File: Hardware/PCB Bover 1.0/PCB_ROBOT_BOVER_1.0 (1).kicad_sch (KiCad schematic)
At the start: 34 parts, among them J1 HC_SRO4, J10 KY_032, J2 HC_SRO4, J3 HC_SRO4, J4 HC_SRO4, J5 Alimentacion, J7 M1, J8 M2, J9 KY_032, U1 L298N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

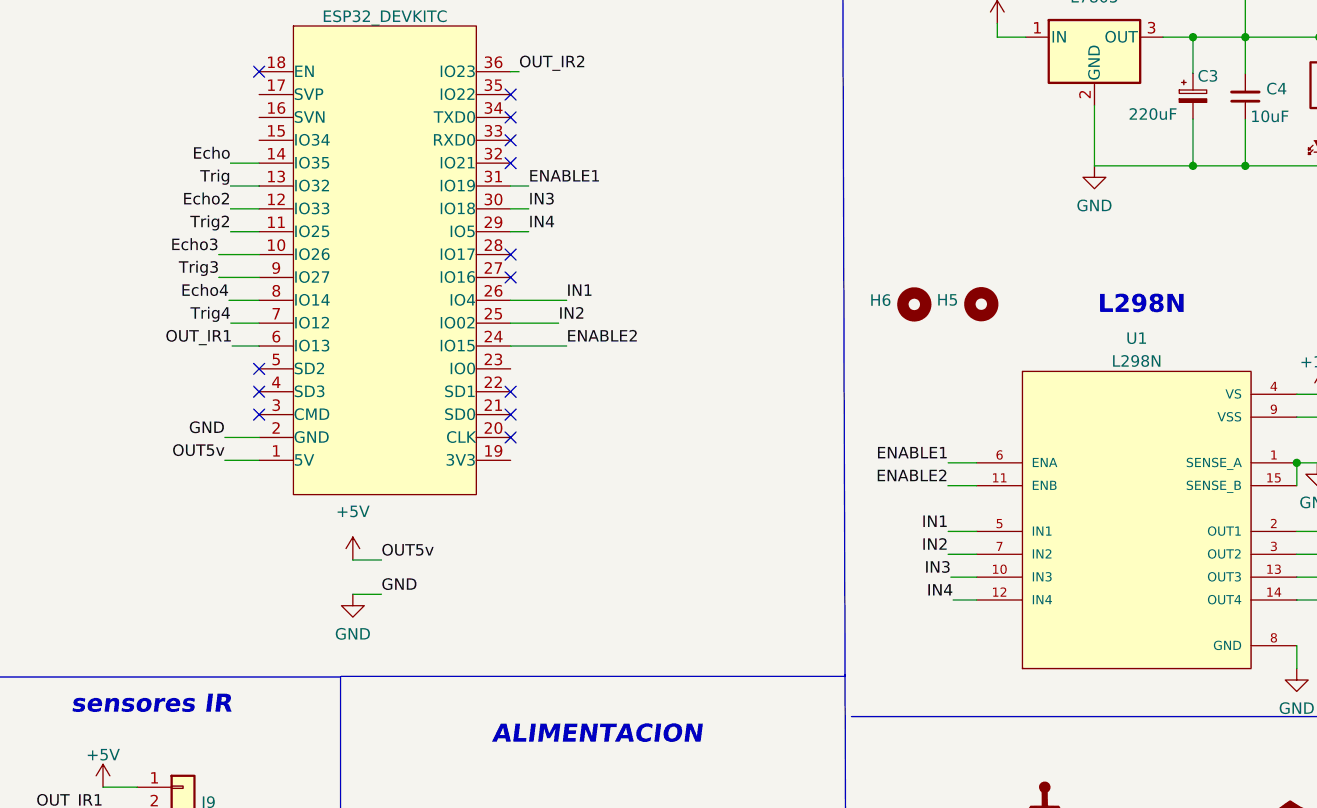
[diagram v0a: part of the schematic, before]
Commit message: add the designs and PCB edit
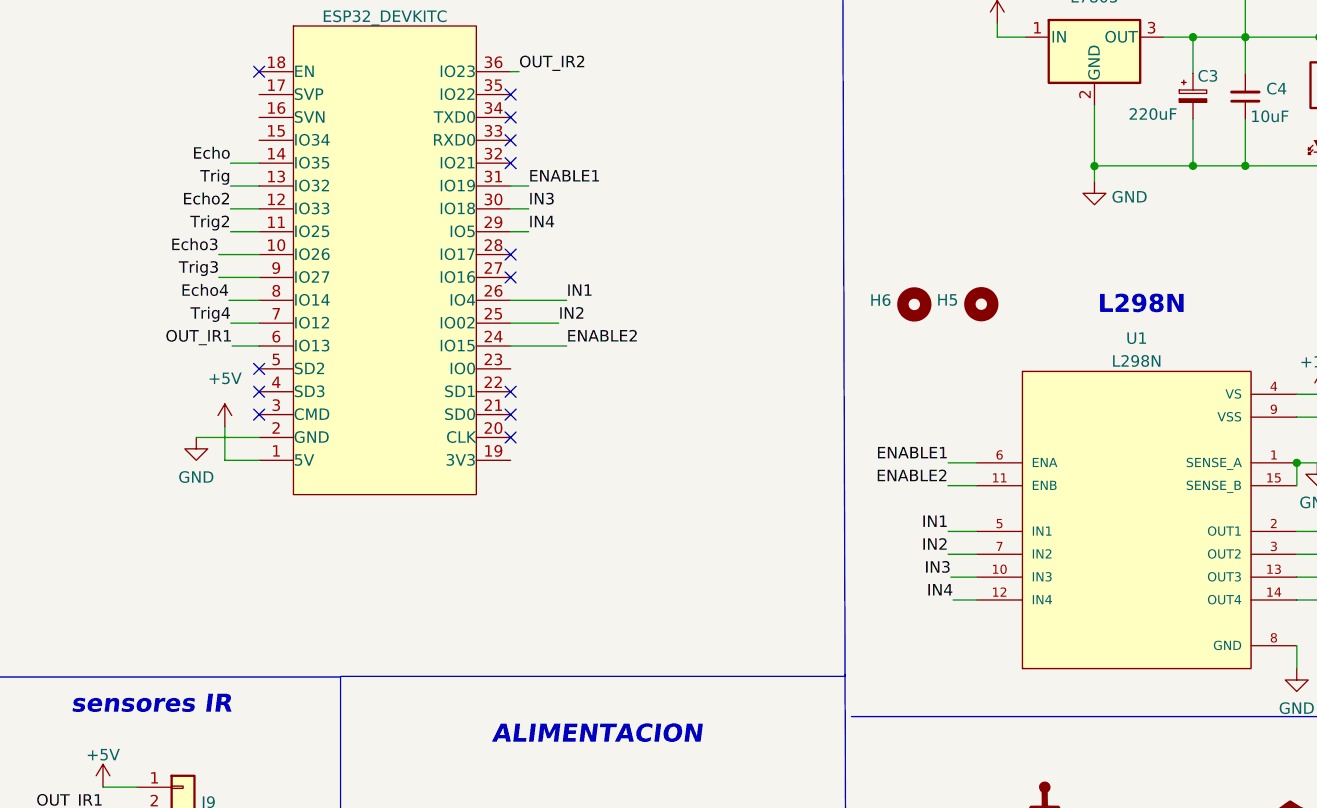
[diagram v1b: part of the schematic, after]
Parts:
- G2: value (none) -> LOGO RB EXP 1.0; footprint (none) -> robot logos:logo rb exp
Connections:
- net GND: no longer C3.2, C4.1, LED1.2 (K), U2.2 (GND)
- new net: C3.2, C4.1, LED1.2 (K), U2.2 (GND)
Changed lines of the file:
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@@
   (junction (at 124.2822 121.1834) (diameter 0) (color 0 0 0 0)
+  )
+  (junction (at 186.69 45.4406) (diameter 0) (color 0 0 0 0)
   )
   (junction (at 252.857 105.791) (diameter 0) (color 0 0 0 0)
@@
     (stroke (width 0) (type default) (color 0 0 0 0))
   )
-  (wire (pts (xy 104.2924 93.0148) (xy 107.4674 93.0148))
-    (stroke (width 0) (type default) (color 0 0 0 0))
-  )
   (wire (pts (xy 248.92 98.7044) (xy 252.857 98.7044))
     (stroke (width 0) (type default) (color 0 0 0 0))
@@
     (stroke (width 0) (type default) (color 0 0 0 0))
   )
+  (wire (pts (xy 186.69 45.4406) (xy 186.69 47.1932))
+    (stroke (width 0) (type default) (color 0 0 0 0))
+  )
   (wire (pts (xy 252.857 110.2868) (xy 260.096 110.2868))
     (stroke (width 0) (type default) (color 0 0 0 0))
@@
     (stroke (width 0) (type default) (color 0 0 0 0))
   )
+  (wire (pts (xy 90.0684 74.422) (xy 90.0684 78.1304))
+    (stroke (width 0) (type default) (color 0 0 0 0))
+  )
   (polyline (pts (xy 158.9786 102.1334) (xy 158.9786 101.981))
     (stroke (width 0) (type default) (color 0 0 0 0))
@@
     (stroke (width 0) (type default) (color 0 0 0 0))
   )
-  (wire (pts (xy 104.2924 89.2048) (xy 107.4674 89.2048))
-    (stroke (width 0) (type default) (color 0 0 0 0))
-  )
   (wire (pts (xy 38.1508 28.8036) (xy 41.783 28.8036))
     (stroke (width 0) (type default) (color 0 0 0 0))
@@
     (stroke (width 0) (type default) (color 0 0 0 0))
   )
-  (wire (pts (xy 90.0684 75.5904) (xy 93.8784 75.5904))
+  (wire (pts (xy 86.8934 75.5904) (xy 93.8784 75.5904))
     (stroke (width 0) (type default) (color 0 0 0 0))
   )
@@
     (effects (font (size 1.27 1.27)) (justify left bottom))
   )
-  (label "GND" (at 90.0684 75.5904 180)
-    (effects (font (size 1.27 1.27)) (justify right bottom))
-  )
   (label "IN2" (at 127.1524 62.8904 0)
     (effects (font (size 1.27 1.27)) (justify left bottom))
   )
-  (label "OUT5v" (at 90.0684 78.1304 180)
-    (effects (font (size 1.27 1.27)) (justify right bottom))
-  )
   (label "OUT1" (at 215.519 86.0298 0)
     (effects (font (size 1.27 1.27)) (justify left bottom))
@@
     (effects (font (size 1.27 1.27)) (justify right bottom))
   )
-  (label "OUT5v" (at 107.4674 89.2048 0)
-    (effects (font (size 1.27 1.27)) (justify left bottom))
-  )
   (label "ENABLE1" (at 170.434 78.4098 180)
     (effects (font (size 1.27 1.27)) (justify right bottom))
@@
   )
   (label "Echo2" (at 41.9862 55.2196 0)
-    (effects (font (size 1.27 1.27)) (justify left bottom))
-  )
-  (label "GND" (at 107.4674 93.0148 0)
     (effects (font (size 1.27 1.27)) (justify left bottom))
   )
@@
       (effects (font (size 1.27 1.27)) hide)
     )
-    (property "Value" "" (id 1) (at 181.6354 135.6489 0)
-      (effects (font (size 1.27 1.27)) hide)
-    )
-    (property "Footprint" "" (id 2) (at 181.6354 124.6378 0)
+    (property "Value" "LOGO RB EXP 1.0" (id 1) (at 181.6354 135.6489 0)
+      (effects (font (size 1.27 1.27)) hide)
+    )
+    (property "Footprint" "robot logos:logo rb exp" (id 2) (at 181.6354 124.6378 0)
       (effects (font (size 1.27 1.27)) hide)
     )
@@
     (pin "1")
   )
-  (symbol (lib_id "power:GND") (at 186.69 45.4152 0) (unit 1)
-    (in_bom yes) (on_board yes) (fields_autoplaced)
-    (property "Reference" "#PWR0131" (id 0) (at 186.69 51.7652 0)
-      (effects (font (size 1.27 1.27)) hide)
-    )
-    (property "Value" "GND" (id 1) (at 186.69 49.8586 0))
-    (property "Footprint" "" (id 2) (at 186.69 45.4152 0)
-      (effects (font (size 1.27 1.27)) hide)
-    )
-    (property "Datasheet" "" (id 3) (at 186.69 45.4152 0)
-      (effects (font (size 1.27 1.27)) hide)
-    )
-    (pin "1")
-  )
   (symbol (lib_id "power:+5V") (at 76.5556 130.1242 0) (unit 1)
     (in_bom yes) (on_board yes) (fields_autoplaced)
@@
     (pin "1")
   )
+  (symbol (lib_id "power:GND") (at 186.69 47.1932 0) (unit 1)
+    (in_bom yes) (on_board yes) (fields_autoplaced)
+    (property "Reference" "#PWR0131" (id 0) (at 186.69 53.5432 0)
+      (effects (font (size 1.27 1.27)) hide)
+    )
+    (property "Value" "GND" (id 1) (at 188.595 48.897 0)
+      (effects (font (size 1.27 1.27)) (justify left))
+    )
+    (property "Footprint" "" (id 2) (at 186.69 47.1932 0)
+      (effects (font (size 1.27 1.27)) hide)
+    )
+    (property "Datasheet" "" (id 3) (at 186.69 47.1932 0)
+      (effects (font (size 1.27 1.27)) hide)
+    )
+    (pin "1")
+  )
   (symbol (lib_id "power:GND") (at 40.767 59.182 0) (unit 1)
     (in_bom yes) (on_board yes) (fields_autoplaced)
@@
     (pin "1")
   )
-  (symbol (lib_id "power:GND") (at 104.2924 93.0148 0) (unit 1)
-    (in_bom yes) (on_board yes) (fields_autoplaced)
-    (property "Reference" "#PWR0122" (id 0) (at 104.2924 99.3648 0)
-      (effects (font (size 1.27 1.27)) hide)
-    )
-    (property "Value" "GND" (id 1) (at 104.2924 97.4582 0))
-    (property "Footprint" "" (id 2) (at 104.2924 93.0148 0)
-      (effects (font (size 1.27 1.27)) hide)
-    )
-    (property "Datasheet" "" (id 3) (at 104.2924 93.0148 0)
+  (symbol (lib_id "power:GND") (at 86.8934 75.5904 0) (unit 1)
+    (in_bom yes) (on_board yes) (fields_autoplaced)
+    (property "Reference" "#PWR0122" (id 0) (at 86.8934 81.9404 0)
+      (effects (font (size 1.27 1.27)) hide)
+    )
+    (property "Value" "GND" (id 1) (at 86.8934 80.0338 0))
+    (property "Footprint" "" (id 2) (at 86.8934 75.5904 0)
+      (effects (font (size 1.27 1.27)) hide)
+    )
+    (property "Datasheet" "" (id 3) (at 86.8934 75.5904 0)
       (effects (font (size 1.27 1.27)) hide)
     )
@@
     (pin "1")
   )
-  (symbol (lib_id "power:+5V") (at 104.2924 89.2048 0) (unit 1)
-    (in_bom yes) (on_board yes) (fields_autoplaced)
-    (property "Reference" "#PWR0111" (id 0) (at 104.2924 93.0148 0)
-      (effects (font (size 1.27 1.27)) hide)
-    )
-    (property "Value" "+5V" (id 1) (at 104.2924 83.8454 0))
-    (property "Footprint" "" (id 2) (at 104.2924 89.2048 0)
-      (effects (font (size 1.27 1.27)) hide)
-    )
-    (property "Datasheet" "" (id 3) (at 104.2924 89.2048 0)
+  (symbol (lib_id "power:+5V") (at 90.0684 74.422 0) (unit 1)
+    (in_bom yes) (on_board yes) (fields_autoplaced)
+    (property "Reference" "#PWR0111" (id 0) (at 90.0684 78.232 0)
+      (effects (font (size 1.27 1.27)) hide)
+    )
+    (property "Value" "+5V" (id 1) (at 90.0684 69.0626 0))
+    (property "Footprint" "" (id 2) (at 90.0684 74.422 0)
+      (effects (font (size 1.27 1.27)) hide)
+    )
+    (property "Datasheet" "" (id 3) (at 90.0684 74.422 0)
       (effects (font (size 1.27 1.27)) hide)
     )
@@
       (reference "#PWR0130") (unit 1) (value "+5V") (footprint "")
     )
-    (path "/38404d84-3920-4014-bb0a-e1f8f6b3830e"
+    (path "/5e79d815-3e66-452c-bc9d-447f9c537736"
       (reference "#PWR0131") (unit 1) (value "GND") (footprint "")
     )
